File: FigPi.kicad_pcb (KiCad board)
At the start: 2 copper layers, 25.8 x 40.4 mm, 45 parts, among them J1 MOLEX_47346-100147346, J2 SPI0 / PWM2 / PWM3, J3 UART0 / PWM3 / PWM4, J4 STEMMA_1/QWIIC_1/I2C1/PMW1, J5 ADC / PWM5 / PWM6, J6 STEMMA_0/QWIIC_0/I2C0/PMW0, J7 PWR, SW1 KMS233GLFG, SW2 KMS233GLFG, U1 RP2040, U2 QSPI NOR FLASH 2MiB 2x3mm USO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, U3 AP2112K-3.3, U4 KC2520Z

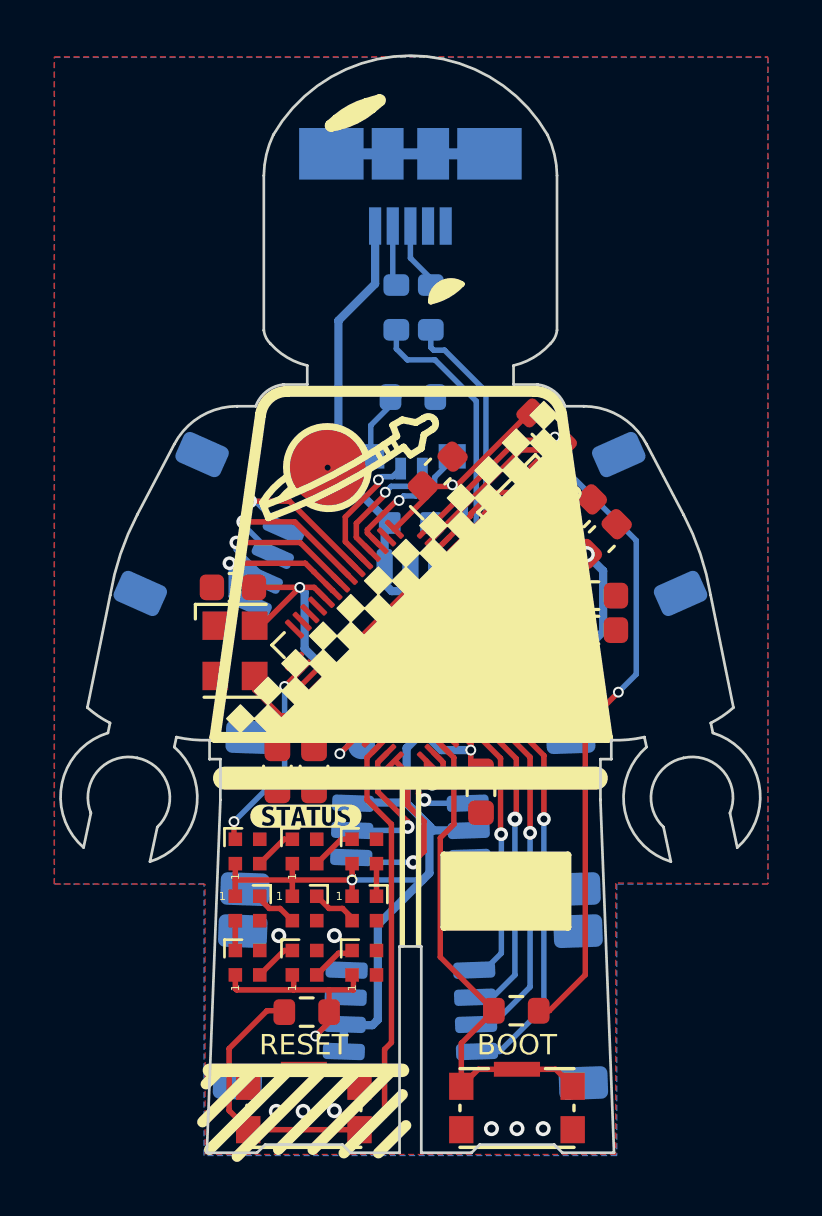
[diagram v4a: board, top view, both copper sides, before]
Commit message: Updated to Rev 2.1 - layout changes, smd size changes.
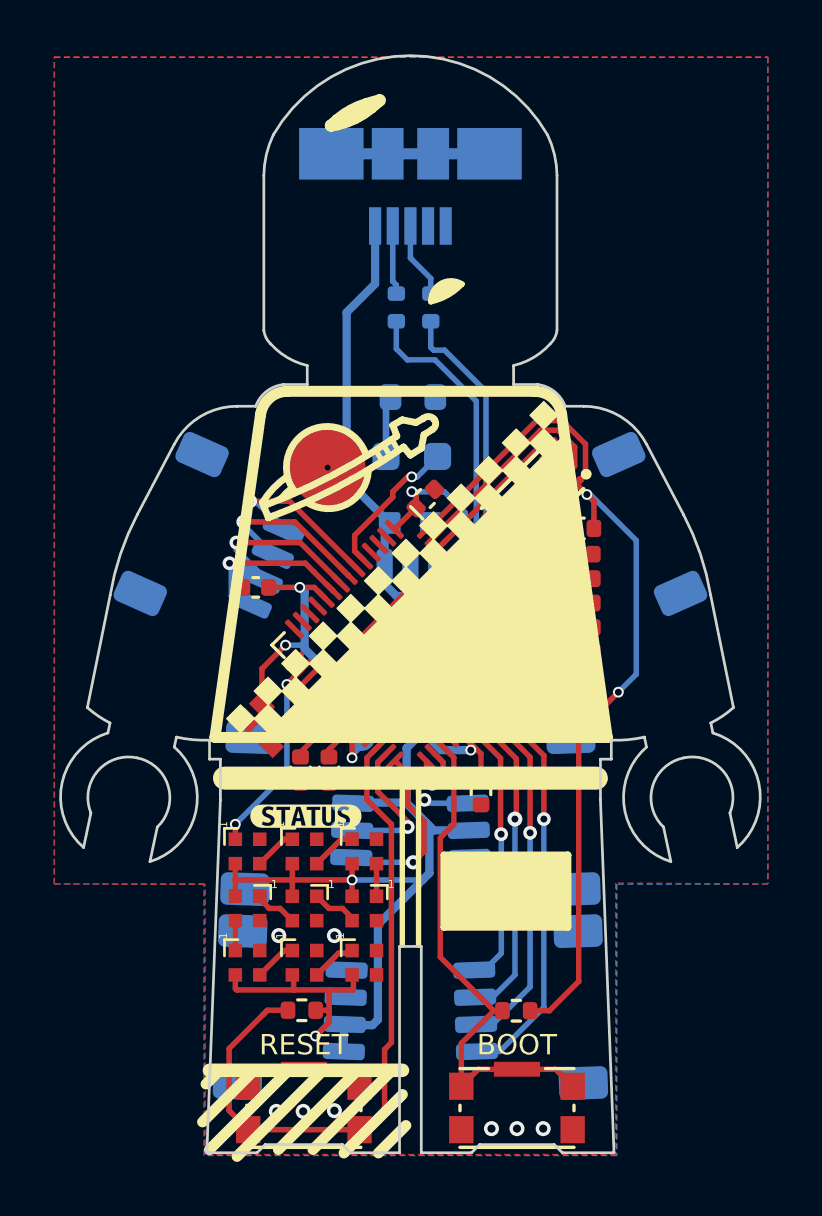
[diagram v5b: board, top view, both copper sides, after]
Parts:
- C1, C11, C12, C13, C14, C3, C5, C6, C7, C8: footprint Capacitor_SMD:C_0603_1608Metric -> Capacitor_SMD:C_0402_1005Metric
- D1: value APFA3010 -> R6C-AM2N2LY; footprint LED_SMD:LED_Kingbright_APFA3010_3x1.5mm_Horizontal -> Custom_Library:LED_1.1x1.7mm
- D10: renamed from D6; value WS2812B -> SK6805; footprint LED_SMD:LED_SK6812_EC15_1.5x1.5mm -> Custom_Library:LED_SK6805_EC15_1.5x1.5mm
- D2: renamed from D4; value WS2812B -> SK6805; footprint LED_SMD:LED_SK6812_EC15_1.5x1.5mm -> Custom_Library:LED_SK6805_EC15_1.5x1.5mm
- D3: renamed from D2; value WS2812B -> SK6805; footprint LED_SMD:LED_SK6812_EC15_1.5x1.5mm -> Custom_Library:LED_SK6805_EC15_1.5x1.5mm
- D4: renamed from D3; value WS2812B -> SK6805; footprint LED_SMD:LED_SK6812_EC15_1.5x1.5mm -> Custom_Library:LED_SK6805_EC15_1.5x1.5mm
- D5: renamed from D7; value WS2812B -> SK6805; footprint LED_SMD:LED_SK6812_EC15_1.5x1.5mm -> Custom_Library:LED_SK6805_EC15_1.5x1.5mm
- D6: renamed from D8; value WS2812B -> SK6805; footprint LED_SMD:LED_SK6812_EC15_1.5x1.5mm -> Custom_Library:LED_SK6805_EC15_1.5x1.5mm
- D7: renamed from D5; value WS2812B -> SK6805; footprint LED_SMD:LED_SK6812_EC15_1.5x1.5mm -> Custom_Library:LED_SK6805_EC15_1.5x1.5mm
- D8: renamed from D12; value WS2812B -> SK6805; footprint LED_SMD:LED_SK6812_EC15_1.5x1.5mm -> Custom_Library:LED_SK6805_EC15_1.5x1.5mm
- D9: renamed from D13; value WS2812B -> SK6805; footprint LED_SMD:LED_SK6812_EC15_1.5x1.5mm -> Custom_Library:LED_SK6805_EC15_1.5x1.5mm
- R1, R2: value 27Ω -> 27.4Ω; footprint Resistor_SMD:R_0603_1608Metric -> Resistor_SMD:R_0402_1005Metric
- R3, R4, R5: footprint Resistor_SMD:R_0603_1608Metric -> Resistor_SMD:R_0402_1005Metric
- R7: value 27R -> 260R
- U2: value QSPI NOR FLASH 2MiB 2x3mm USON (W25Q16JVUXIM) -> QSPI NOR FLASH 2MiB 2x3mm USON (W25Q16JVUXIQ); footprint MINI_SAM_D51_r025_b001:USON8 -> Custom_Library:USON-8_L3.0-W2.0-P0.50-BL-EP
- U4: value KC2520Z -> OT201612MJBA4SL; footprint Oscillator:Oscillator_SMD_Kyocera_KC2520Z-4Pin_2.5x2.0mm -> Custom_Library:Oscillator_SMD_Yangzing_Tech_SMD2016-4P
- moved R4 3.87 mm to (18.2, -23.0), turned to 0 degrees
- moved U4 2.98 mm to (6.70, -15.8), turned to -45 degrees
- moved C5 1.66 mm to (18.2, -21.1), turned to 180 degrees
- moved C2 1.57 mm to (18.2, -20.2), turned to 0 degrees
- moved C1 1.47 mm to (18.2, -22.1), turned to 180 degrees
- moved C6 1.29 mm to (18.2, -19.4)
- moved C11 1.09 mm to (12.6, -24.1)
- moved C13 0.97 mm to (18.2, -18.4)
- moved C8 0.85 mm to (7.95, -14.1)
- moved C7 0.84 mm to (6.30, -20.8)
- moved C3 0.55 mm to (9.00, -14.1)
- moved C14 0.41 mm to (18.2, -17.6), turned to 180 degrees
- moved TP1 0.30 mm to (10.2, -15.3)
- moved U2 0.29 mm to (16.5, -24.1), turned to 135 degrees
- moved R5 0.19 mm to (8.00, -5.25)
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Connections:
- D1 pad 1: /LED_R -> Net-(D1-Pad1)
- D1 pad 2: Net-(D1-Pad2) -> /LED_G
- D10 pad 1: +3V3 -> Net-(D10-Pad1)
- D10 pad 2: unconnected-(D6-Pad2) -> +3V3
- D10 pad 3: GND -> unconnected-(D10-Pad3)
- D10 pad 4: Net-(D5-Pad2) -> GND
- D2 pad 1: +3V3 -> /RGB_DIN
- D2 pad 2: Net-(D4-Pad2) -> +3V3
- D2 pad 3: GND -> Net-(D2-Pad3)
- D2 pad 4: /RGB_DIN -> GND
- D3 pad 1: +3V3 -> Net-(D3-Pad1)
- D3 pad 2: Net-(D2-Pad2) -> +3V3
- D3 pad 3: GND -> Net-(D3-Pad3)
- D3 pad 4: Net-(D12-Pad2) -> GND
- D4 pad 1: +3V3 -> Net-(D4-Pad1)
- D4 pad 2: Net-(D3-Pad2) -> +3V3
- D4 pad 3: GND -> Net-(D4-Pad3)
- D4 pad 4: Net-(D13-Pad2) -> GND
- D5 pad 1: +3V3 -> Net-(D2-Pad3)
- D5 pad 2: Net-(D12-Pad4) -> +3V3
- D5 pad 3: GND -> Net-(D5-Pad3)
- D5 pad 4: Net-(D4-Pad2) -> GND
- D6 pad 1: +3V3 -> Net-(D3-Pad3)
- D6 pad 2: Net-(D13-Pad4) -> +3V3
- D6 pad 3: GND -> Net-(D6-Pad3)
- D6 pad 4: Net-(D2-Pad2) -> GND
- D7 pad 1: +3V3 -> Net-(D4-Pad3)
- D7 pad 2: Net-(D5-Pad2) -> +3V3
- D7 pad 3: GND -> Net-(D10-Pad1)
- D7 pad 4: Net-(D3-Pad2) -> GND
- D8 pad 1: +3V3 -> Net-(D5-Pad3)
- D8 pad 2: Net-(D12-Pad2) -> +3V3
- D8 pad 3: GND -> Net-(D3-Pad1)
- D8 pad 4: Net-(D12-Pad4) -> GND
- D9 pad 1: +3V3 -> Net-(D6-Pad3)
- D9 pad 2: Net-(D13-Pad2) -> +3V3
- D9 pad 3: GND -> Net-(D4-Pad1)
- D9 pad 4: Net-(D13-Pad4) -> GND
- R7 pad 1: Net-(D1-Pad2) -> Net-(D1-Pad1)
- U1 pad 3: /LED_R -> unconnected-(U1-Pad3)
- U1 pad 4: /LED_B -> unconnected-(U1-Pad4)
- U2 pad 8: /VDD -> +3V3
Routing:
- net /LED_R: track 5.24 -> 0.00 mm, vias 1 -> 0
- net /LED_B: track 4.68 -> 0.00 mm, vias 1 -> 0
- net +3V3: track 107.5 -> 103.5 mm, vias 8 -> 10
- net Net-(D1-Pad2): track 2.62 -> 0.00 mm
- net Net-(D1-Pad1): track 0.00 -> 2.26 mm
- net /QSPI_DATA[2]: track 4.92 -> 6.89 mm
- net Net-(U1-Pad20): track 4.04 -> 2.17 mm
- net Net-(D3-Pad3): track 0.00 -> 1.77 mm
- net Net-(D2-Pad2): track 1.77 -> 0.00 mm
- net Net-(D6-Pad3): track 0.00 -> 1.67 mm
- net Net-(D5-Pad3): track 0.00 -> 1.67 mm
- net Net-(D13-Pad4): track 1.67 -> 0.00 mm
- net Net-(D12-Pad4): track 1.67 -> 0.00 mm
- net Net-(D5-Pad2): track 1.63 -> 0.00 mm
- net Net-(D10-Pad1): track 0.00 -> 1.63 mm
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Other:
- board text added: "Fig Pi v2.1"
- board text removed: "Fig Pi v1.7"

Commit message: modified:   FigPi.kicad_pcb modified:   FigPi.kicad_sch
Swapped around the stemma connector pins.
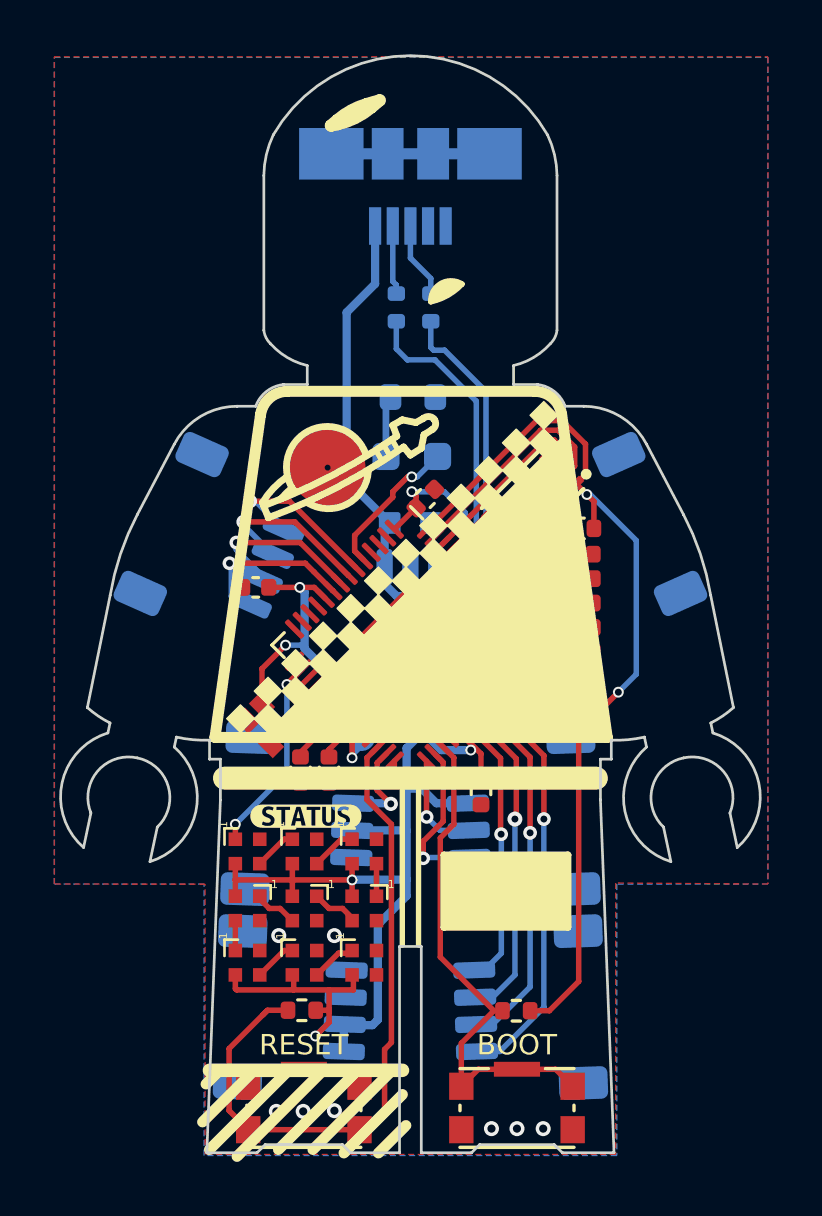
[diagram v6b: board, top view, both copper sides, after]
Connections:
- net /RGB_DIN renamed NEO_DIN
- J4 pad 1: /SCL1 -> GND
- J4 pad 2: /SDA1 -> +3V3
- J4 pad 3: +3V3 -> /SDA1
- J4 pad 4: GND -> /SCL1
- J6 pad 1: /SCL/D5 -> GND
- J6 pad 2: /SDA/D4 -> +3V3
- J6 pad 3: +3V3 -> /SDA/D4
- J6 pad 4: GND -> /SCL/D5
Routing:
- net /SCL/D5: track 6.64 -> 2.27 mm
- net /SCL1: track 2.82 -> 6.03 mm
- net /SDA/D4: track 5.40 -> 3.64 mm
- net +3V3: track 103.5 -> 102.0 mm
- net /SDA1: track 3.29 -> 3.82 mm
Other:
- board text added: "Fig Pi v2.2"
- board text removed: "Fig Pi v2.1"

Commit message: Update to v2.3
Updated the schematic and board to v2.3.
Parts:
- removed the J1 at (12.0, -36.8)
- removed kibuzzard-620D4CA4: G***, kibuzzard-620D4CA4
- added D11: RB520S-30, Diode_SMD:D_SOD-523, F.Cu at (15.9, -6.00)
- added J7: USB_B_Micro, Connector_USB:USB_Micro-B_Molex_47346-0001, B.Cu at (12.0, -35.6)
- added kibuzzard-640B746F: G***, kibuzzard-640B746F, F.Cu at (8.35, -12.7)
- added kibuzzard-640F7A39: G***, kibuzzard-640F7A39, B.Cu at (16.1, -16.5)
- added kibuzzard-640F7A5B: G***, kibuzzard-640F7A5B, B.Cu at (8.12, -16.5)
- added kibuzzard-640F7BF6: G***, kibuzzard-640F7BF6, B.Cu at (17.4, -26.2)
- added kibuzzard-640F7C1A: G***, kibuzzard-640F7C1A, B.Cu at (6.47, -26.4)
- added kibuzzard-640F7C6F: G***, kibuzzard-640F7C6F, B.Cu at (7.67, -1.18)
- added kibuzzard-640F7C7F: G***, kibuzzard-640F7C7F, B.Cu at (16.8, -1.15)
- added kibuzzard-640F7D7C: G***, kibuzzard-640F7D7C, B.Cu at (9.18, -32.5)
- C4: renamed from C9; footprint MINI_SAM_D51_r025_b001:0603_CAPACITOR -> Resistor_SMD:R_0603_1608Metric
- C5: renamed from C10; footprint MINI_SAM_D51_r025_b001:0603_CAPACITOR -> Resistor_SMD:R_0603_1608Metric
- SW1, SW2: value KMS233GLFG -> KMS231GLFG
- U2: value QSPI NOR FLASH 2MiB 2x3mm USON (W25Q16JVUXIQ) -> QSPI NOR FLASH 2MiB 2x3mm USON (W25Q16JVUXxQ)
- moved TP2 2.47 mm to (12.2, -15.2)
- moved R6 1.97 mm to (15.9, -7.20)
- moved C1 0.52 mm to (17.7, -22.1)
- moved C8 0.50 mm to (6.80, -20.8)
- moved C6 0.40 mm to (17.9, -21.1)
- moved C11 0.39 mm to (14.4, -13.7)
- moved C10 0.37 mm to (12.7, -24.4)
- moved C2 0.27 mm to (18.0, -20.2)
- moved C7 0.15 mm to (18.1, -19.4)
- moved C13 0.10 mm to (18.4, -17.6)
- moved R2 0.08 mm to (8.07, -5.28), turned to 0 degrees
- turned D10 to 180 degrees
- turned R1 to 180 degrees
- renumbered C11 to C10, C12 to C11, C13 to C12, C14 to C13, C5 to C6, C6 to C7, C7 to C8, C8 to C9, D2 to D1, D1 to D10, D5 to D2, D8 to D3, D3 to D4, D6 to D5, D9 to D6, D4 to D7, D7 to D8, D10 to D9, J7 to J1, J6 to J3, J3 to J5, J5 to J6, R7 to R1, R5 to R2, R4 to R3, R2 to R4, R1 to R5, R3 to R6, U4 to U3, U3 to U4
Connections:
- net /QSPI_CS renamed QSPI_CS
- net /QSPI_DATA[0] renamed QSPI_SD0
- net /QSPI_DATA[1] renamed QSPI_SD1
- net /QSPI_DATA[2] renamed QSPI_SD2
- net /QSPI_DATA[3] renamed QSPI_SD3
- net /QSPI_SCK renamed QSPI_SCK
- net /USBD+ renamed USBD+
- net /USBD- renamed USBD-
- net /VBUS renamed VBUS
- C10 pad 2: +3V3 -> +3.3V
- C11 pad 2: +3V3 -> +3.3V
- C12 pad 2: +3V3 -> +3.3V
- C13 pad 2: +3V3 -> +3.3V
- C5 pad 1: +3V3 -> +3.3V
- C6 pad 2: +3V3 -> +3.3V
- C7 pad 2: +3V3 -> +3.3V
- C8 pad 2: +3V3 -> +3.3V
- C9 pad 2: +3V3 -> +3.3V
- D1 pad 2: +3V3 -> +3.3V
- D10 pad 2: /LED_G -> LED
- D2 pad 2: +3V3 -> +3.3V
- D3 pad 2: +3V3 -> +3.3V
- D4 pad 2: +3V3 -> +3.3V
- D5 pad 2: +3V3 -> +3.3V
- D6 pad 2: +3V3 -> +3.3V
- D7 pad 2: +3V3 -> +3.3V
- D8 pad 2: +3V3 -> +3.3V
- D9 pad 2: +3V3 -> +3.3V
- J1 pad 1: +3V3 -> +3.3V
- J1 pad 2: +3V3 -> +3.3V
- J2 pad 1: /MOSI/D10 -> /MISO/D9
- J2 pad 2: /SCK/D8 -> /D14
- J2 pad 3: /D14 -> /SCK/D8
- J2 pad 4: /MISO/D9 -> /MOSI/D10
- J3 pad 2: +3V3 -> +3.3V
- J4 pad 2: +3V3 -> +3.3V
- R2 pad 1: +3V3 -> ~{RESET}
- R2 pad 2: /RUN -> +3.3V
- R3 pad 1: +3V3 -> +3.3V
- R6 pad 1: /~{USB_BOOT} -> Net-(D11-Pad2)
- SW1 pad 1: /RUN -> GND
- SW1 pad 2: GND -> ~{RESET}
- SW1 pad 3: GND -> ~{RESET}
- SW1 pad 4: GND -> ~{RESET}
- SW1 pad 5: /RUN -> GND
- SW2 pad 2: /~{USB_BOOT} -> BUTTON
- SW2 pad 3: /~{USB_BOOT} -> BUTTON
- SW2 pad 4: /~{USB_BOOT} -> BUTTON
- U1 pad 1: +3V3 -> +3.3V
- U1 pad 10: +3V3 -> +3.3V
- U1 pad 2: unconnected-(U1-Pad2) -> LED
- U1 pad 22: +3V3 -> +3.3V
- U1 pad 26: /RUN -> ~{RESET}
- U1 pad 31: /~{USB_BOOT} -> BUTTON
- U1 pad 33: +3V3 -> +3.3V
- U1 pad 42: +3V3 -> +3.3V
- U1 pad 43: +3V3 -> +3.3V
- U1 pad 44: +3V3 -> +3.3V
- U1 pad 48: +3V3 -> +3.3V
- U1 pad 49: +3V3 -> +3.3V
- U1 pad 5: /LED_G -> unconnected-(U1-Pad5)
- U2 pad 8: +3V3 -> +3.3V
- U3 pad 4: +3V3 -> +3.3V
- U4 pad 5: +3V3 -> +3.3V
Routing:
- net +3V3: track 102.0 -> 0.00 mm, vias 10 -> 0
- net +3.3V: track 0.00 -> 98.4 mm, vias 0 -> 9
- net /RUN: track 25.8 -> 0.00 mm
- net BUTTON: track 0.00 -> 21.1 mm
- net ~{RESET}: track 0.00 -> 20.6 mm
- net /~{USB_BOOT}: track 19.0 -> 0.00 mm
- net /LED_G: track 5.42 -> 0.00 mm, vias 1 -> 0
- net /SCK/D8: track 6.19 -> 2.55 mm
- net LED: track 0.00 -> 3.63 mm, vias 0 -> 1
- net /MOSI/D10: track 6.31 -> 3.21 mm
- net QSPI_CS: track 32.9 -> 30.8 mm
- net /MISO/D9: track 6.59 -> 8.60 mm
- net Net-(D11-Pad2): track 0.00 -> 1.28 mm
- net +1V2: track 18.4 -> 17.3 mm
- net GND: track 5.85 -> 6.23 mm, vias 13 -> 12
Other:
- rule pad_to_mask_clearance: 0.0508 -> 0
- board text added: "+"
- board text added: "-"
- board text added: "BOOT/BTN"
- board text added: "Fig Pi v2.3"
- board text removed: "BOOT"
- board text removed: "Fig Pi v2.2"

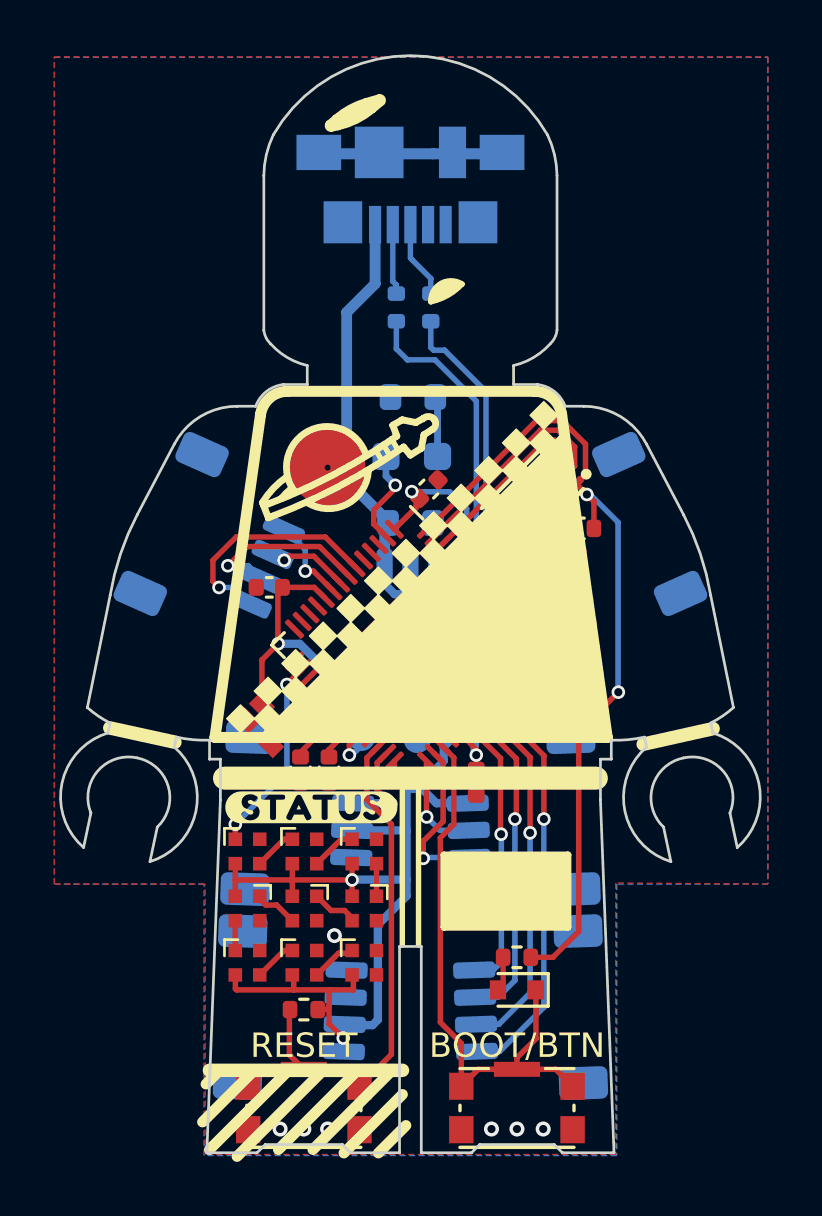
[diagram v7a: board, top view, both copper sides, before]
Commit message: Updated Bottom Silkscreen
Changed the I2C connector labels.
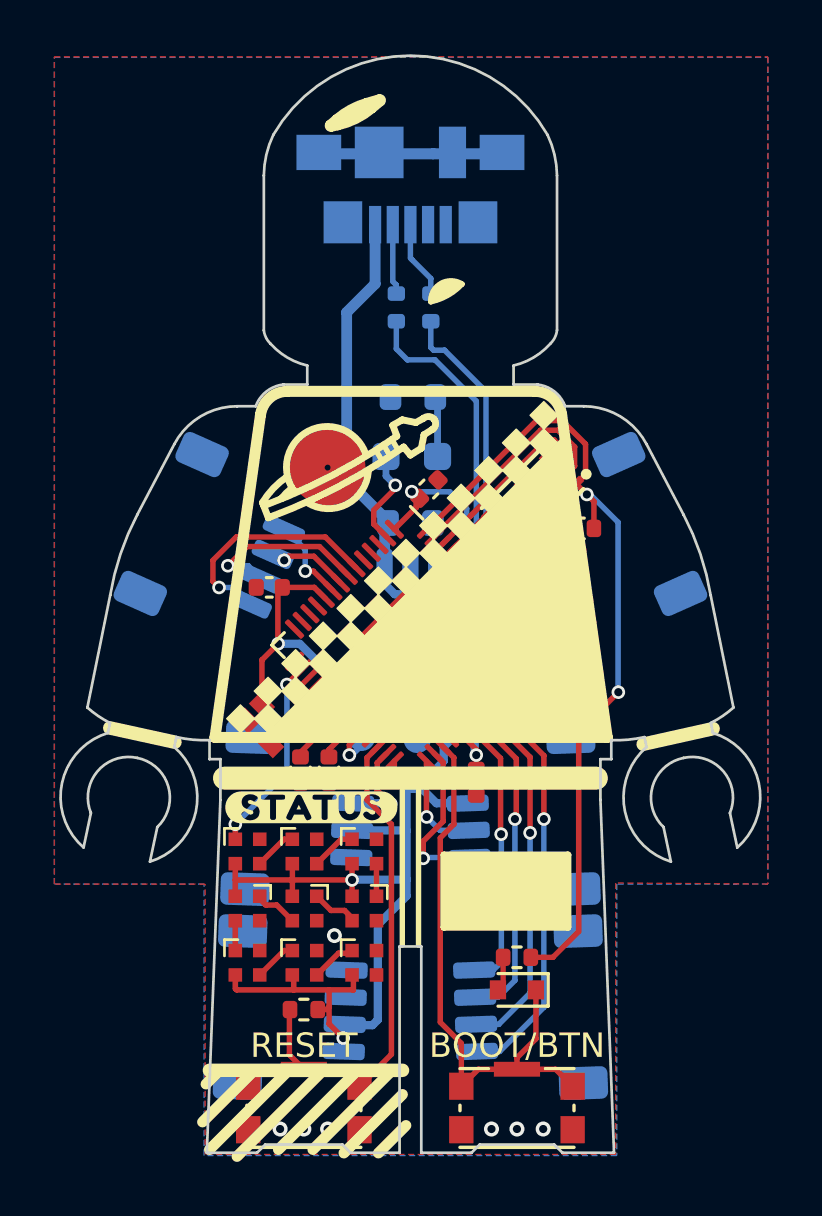
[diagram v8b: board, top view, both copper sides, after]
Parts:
- removed kibuzzard-640F7A39: G***, kibuzzard-640F7A39
- removed kibuzzard-640F7A5B: G***, kibuzzard-640F7A5B
- added kibuzzard-6411F9C1: G***, kibuzzard-6411F9C1, B.Cu at (16.1, -16.5)
- added kibuzzard-6411FA03: G***, kibuzzard-6411FA03, B.Cu at (8.12, -16.5)
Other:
- board text added: "Fig Pi v2.3.1"
- board text removed: "Fig Pi v2.3"
